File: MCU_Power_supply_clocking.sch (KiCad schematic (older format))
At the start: 60 parts, among them J2 OSTTC020162, J3 OSTTC020162, U10 TLV75529PDBV, U11 STM32H743ZIT6, U12 LD1117S33CTR, U13 LD1117S33CTR, U9 ST1L05APU33R, Y1 NX5032GA-8MHz, Y2 NX3215SA-32.768K-STD-MUA-14

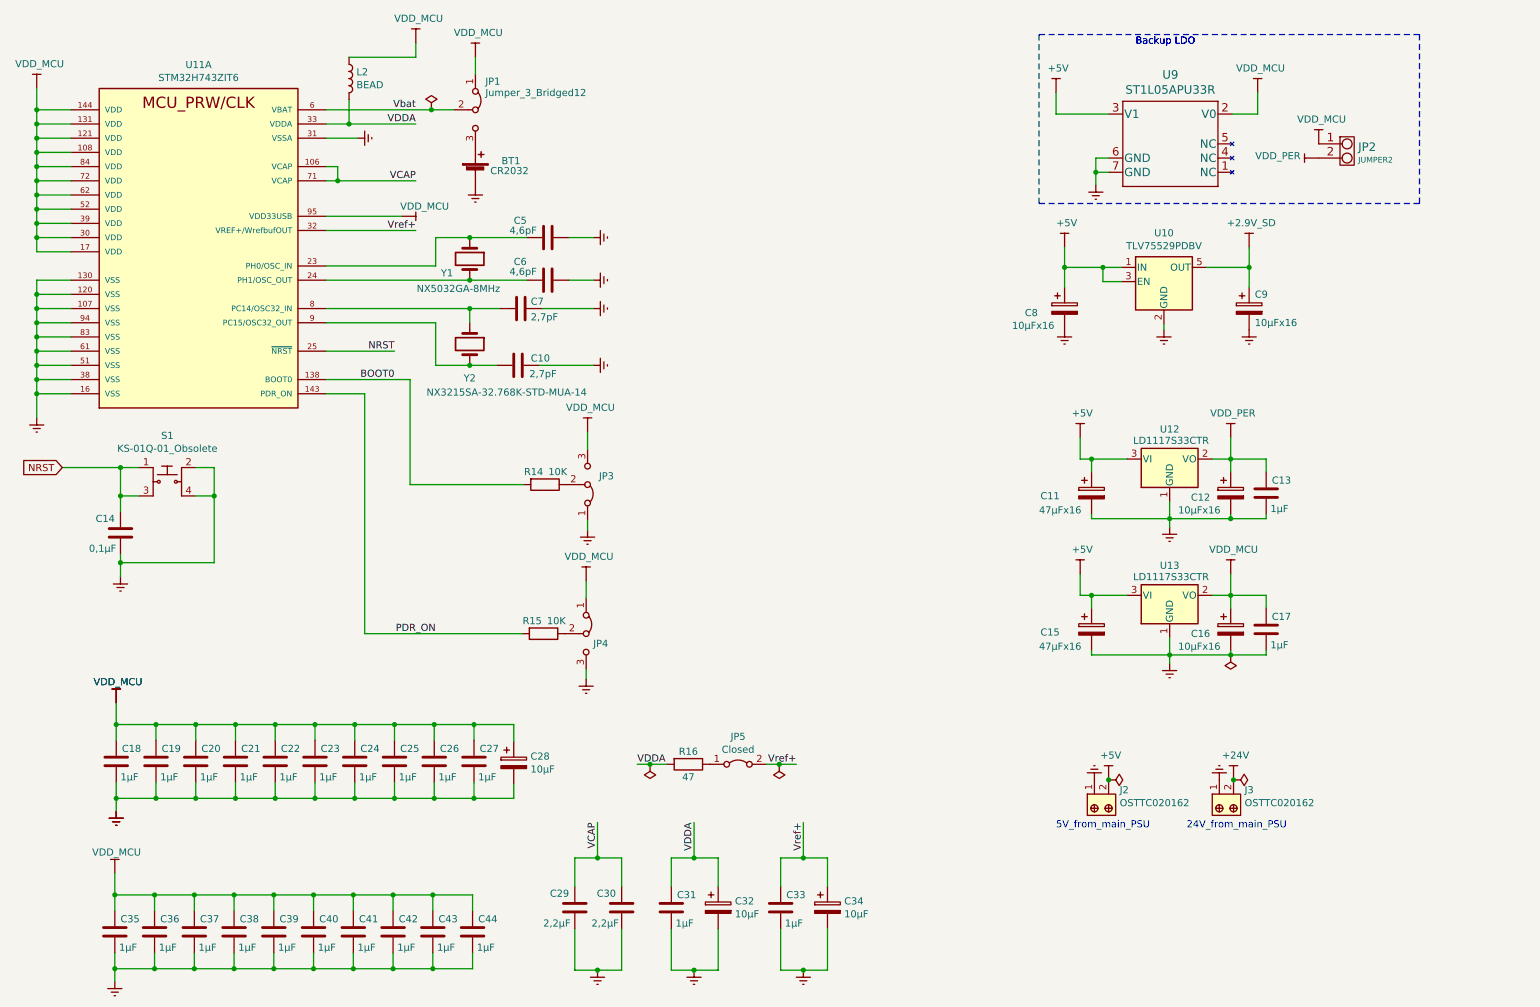
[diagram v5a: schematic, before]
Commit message: footprints associations is done
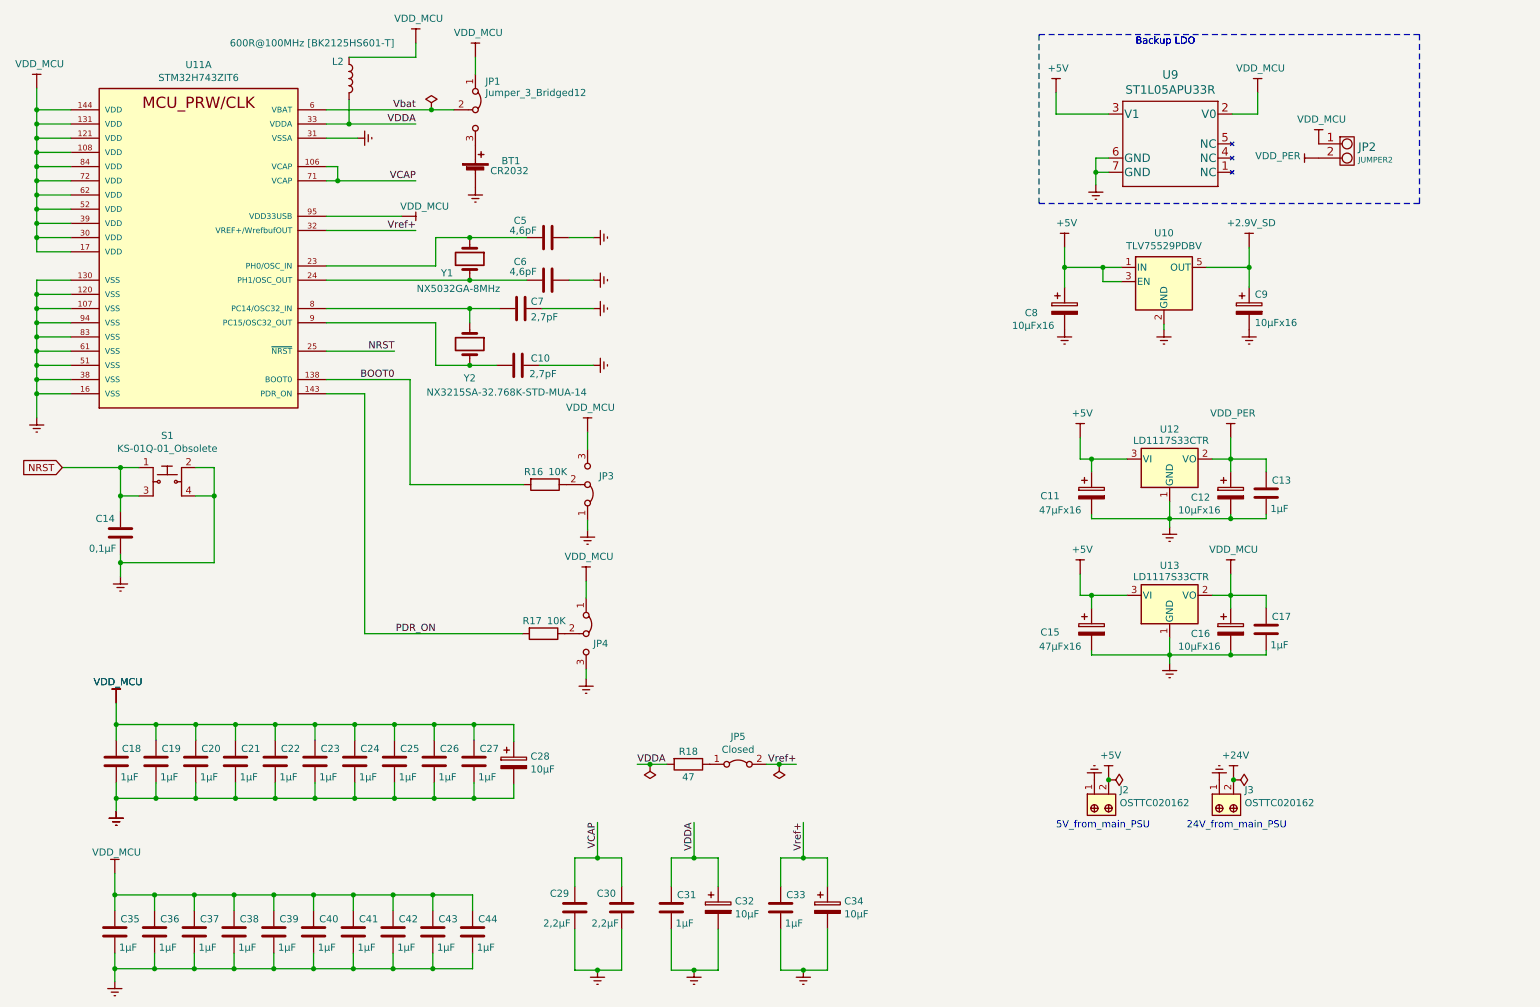
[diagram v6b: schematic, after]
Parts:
- C29, C30: footprint Capacitor_SMD:C_0805_2012Metric_Pad1.18x1.45mm_HandSolder -> Capacitor_SMD:C_0603_1608Metric_Pad1.08x0.95mm_HandSolder; Type C2012X7R1H225KT000E -> GRM188Z71E225KE43D
- JP1, JP4: footprint (none) -> Jumper:SolderJumper-3_P1.3mm_Open_RoundedPad1.0x1.5mm_NumberLabels
- JP2: footprint (none) -> Jumper:SolderJumper-2_P1.3mm_Open_TrianglePad1.0x1.5mm
- JP3: footprint (none) -> Connector_PinHeader_2.54mm:PinHeader_1x03_P2.54mm_Horizontal
- JP5: footprint (none) -> Jumper:SolderJumper-2_P1.3mm_Open_RoundedPad1.0x1.5mm
- L2: value BEAD -> 600R@100MHz [BK2125HS601-T]; footprint (none) -> Inductor_SMD:L_0805_2012Metric_Pad1.15x1.40mm_HandSolder
- U11: footprint QFP50P2200X2200X160-144N -> SVIELCOM:QFP50P2200X2200X160-144N
- U9: footprint DFN_5APU33R_STM -> SVIELCOM:ST1L05APU33R
- renumbered R14 to R16, R15 to R17, R16 to R18
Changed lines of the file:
@@
 Title "ШВУ"
 Date "2021-03-25"
-Rev "V0.1"
+Rev "V0.3"
 Comp "ЦВЕТМЕТНАЛАДКА"
 Comment1 "Шустов В.И."
@@
 F 0 "C29" H 4540 6770 50  0000 L CNN
 F 1 "2,2µF" H 4530 6980 50  0000 L CNN
-F 2 "Capacitor_SMD:C_0805_2012Metric_Pad1.18x1.45mm_HandSolder" H 4538 6720 50  0001 C CNN
+F 2 "Capacitor_SMD:C_0603_1608Metric_Pad1.08x0.95mm_HandSolder" H 4538 6720 50  0001 C CNN
 F 3 "" H 4500 6870 50  0001 C CNN
-F 4 "C2012X7R1H225KT000E" H 4500 6870 50  0001 C CNN "Type"
+F 4 "GRM188Z71E225KE43D" H 4500 6870 50  0001 C CNN "Type"
 	1    4500 6870
 	-1   0    0    1
@@
 F 0 "U11" H 1850 4267 50  0000 C CNN
 F 1 "STM32H743ZIT6" H 1850 4176 50  0000 C CNN
-F 2 "QFP50P2200X2200X160-144N" H 1900 4200 50  0001 L BNN
+F 2 "SVIELCOM:QFP50P2200X2200X160-144N" H 1900 4200 50  0001 L BNN
 F 3 "" H 1900 4600 50  0001 L BNN
 F 4 "STMicroelectronics" H 1900 4300 50  0001 L BNN "MANUFACTURER"
@@
 P 4290 3890
 AR Path="/60A0FE86" Ref="R?"  Part="1"
-AR Path="/60A03F8A/60A0FE86" Ref="R14"  Part="1"
-F 0 "R14" V 4200 3810 50  0000 C CNN
+AR Path="/60A03F8A/60A0FE86" Ref="R16"  Part="1"
+F 0 "R16" V 4200 3810 50  0000 C CNN
 F 1 "10K" V 4200 3980 50  0000 C CNN
 F 2 "Resistor_SMD:R_0805_2012Metric_Pad1.20x1.40mm_HandSolder" V 4220 3890 50  0001 C CNN
@@
 F 0 "C30" H 4870 6770 50  0000 L CNN
 F 1 "2,2µF" H 4850 6980 50  0000 L CNN
-F 2 "Capacitor_SMD:C_0805_2012Metric_Pad1.18x1.45mm_HandSolder" H 4868 6720 50  0001 C CNN
+F 2 "Capacitor_SMD:C_0603_1608Metric_Pad1.08x0.95mm_HandSolder" H 4868 6720 50  0001 C CNN
 F 3 "" H 4830 6870 50  0001 C CNN
-F 4 "C2012X7R1H225KT000E" H 4830 6870 50  0001 C CNN "Type"
+F 4 "GRM188Z71E225KE43D" H 4830 6870 50  0001 C CNN "Type"
 	1    4830 6870
 	-1   0    0    1
@@
 F 0 "JP1" V 3600 1320 50  0000 L CNN
 F 1 "Jumper_3_Bridged12" V 3680 1320 50  0000 L CNN
-F 2 "" H 3800 1250 50  0001 C CNN
+F 2 "Jumper:SolderJumper-3_P1.3mm_Open_RoundedPad1.0x1.5mm_NumberLabels" H 3800 1250 50  0001 C CNN
 F 3 "~" H 3800 1250 50  0001 C CNN
 	1    3800 1250
@@
 F 0 "JP3" V 4650 3970 50  0000 L CNN
 F 1 "Jumper_3_Bridged12" V 4580 3990 50  0001 L CNN
-F 2 "" H 4590 3890 50  0001 C CNN
+F 2 "Connector_PinHeader_2.54mm:PinHeader_1x03_P2.54mm_Horizontal" H 4590 3890 50  0001 C CNN
 F 3 "~" H 4590 3890 50  0001 C CNN
 	1    4590 3890
@@
 F 0 "JP5" H 5650 6055 50  0000 C CNN
 F 1 "Closed" H 5650 5964 50  0000 C CNN
-F 2 "" H 5650 5860 50  0001 C CNN
+F 2 "Jumper:SolderJumper-2_P1.3mm_Open_RoundedPad1.0x1.5mm" H 5650 5860 50  0001 C CNN
 F 3 "~" H 5650 5860 50  0001 C CNN
 	1    5650 5860
@@
 P 4280 4940
 AR Path="/60A0FEB9" Ref="R?"  Part="1"
-AR Path="/60A03F8A/60A0FEB9" Ref="R15"  Part="1"
-F 0 "R15" V 4190 4860 50  0000 C CNN
+AR Path="/60A03F8A/60A0FEB9" Ref="R17"  Part="1"
+F 0 "R17" V 4190 4860 50  0000 C CNN
 F 1 "10K" V 4190 5030 50  0000 C CNN
 F 2 "Resistor_SMD:R_0805_2012Metric_Pad1.20x1.40mm_HandSolder" V 4210 4940 50  0001 C CNN
@@
 F 0 "JP4" V 4650 4990 50  0000 L CNN
 F 1 "Jumper_3_Bridged12" V 4570 5040 50  0001 L CNN
-F 2 "" H 4580 4940 50  0001 C CNN
+F 2 "Jumper:SolderJumper-3_P1.3mm_Open_RoundedPad1.0x1.5mm_NumberLabels" H 4580 4940 50  0001 C CNN
 F 3 "~" H 4580 4940 50  0001 C CNN
 	1    4580 4940
@@
 F 0 "U9" H 8695 2177 60  0000 C CNN
 F 1 "ST1L05APU33R" H 8695 2071 60  0000 C CNN
-F 2 "DFN_5APU33R_STM" H 8860 2030 60  0001 C CNN
+F 2 "SVIELCOM:ST1L05APU33R" H 8860 2030 60  0001 C CNN
 F 3 "https://my.st.com/resource/en/datasheet/st1l05.pdf" H 8695 2071 60  0001 C CNN
 	1    8060 1590
@@
 F 0 "JP2" H 10018 1468 60  0000 L CNN
 F 1 "JUMPER2" H 10018 1377 40  0000 L CNN
-F 2 "" H 10040 1490 60  0001 C CNN
+F 2 "Jumper:SolderJumper-2_P1.3mm_Open_TrianglePad1.0x1.5mm" H 10040 1490 60  0001 C CNN
 F 3 "" H 10040 1490 60  0000 C CNN
 	1    10040 1490
@@
 P 5300 5860
 AR Path="/60D1EBF4" Ref="R?"  Part="1"
-AR Path="/60A03F8A/60D1EBF4" Ref="R16"  Part="1"
-F 0 "R16" V 5210 5860 50  0000 C CNN
+AR Path="/60A03F8A/60D1EBF4" Ref="R18"  Part="1"
+F 0 "R18" V 5210 5860 50  0000 C CNN
 F 1 "47" V 5390 5860 50  0000 C CNN
 F 2 "Resistor_SMD:R_0805_2012Metric_Pad1.20x1.40mm_HandSolder" V 5230 5860 50  0001 C CNN
@@
 AR Path="/60A0FE91" Ref="L?"  Part="1"
 AR Path="/60A03F8A/60A0FE91" Ref="L2"  Part="1"
-F 0 "L2" H 2962 1076 50  0000 L CNN
-F 1 "BEAD" H 2962 985 50  0000 L CNN
-F 2 "" H 2910 1030 50  0001 C CNN
+F 0 "L2" H 2790 1150 50  0000 L CNN
+F 1 "600R@100MHz [BK2125HS601-T]" H 2070 1280 50  0000 L CNN
+F 2 "Inductor_SMD:L_0805_2012Metric_Pad1.15x1.40mm_HandSolder" H 2910 1030 50  0001 C CNN
 F 3 "~" H 2910 1030 50  0001 C CNN
 	1    2910 1030
@@
 	3020 4940 4130 4940
 $Comp
-L power:PWR_FLAG #FLG08
+L power:PWR_FLAG #FLG07
 U 1 1 610DFDF1
 P 8260 5970
-F 0 "#FLG08" H 8260 6045 50  0001 C CNN
+F 0 "#FLG07" H 8260 6045 50  0001 C CNN
 F 1 "PWR_FLAG" V 8260 6098 50  0001 L CNN
 F 2 "" H 8260 5970 50  0001 C CNN
@@
 Connection ~ 8260 5970
 $Comp
-L power:PWR_FLAG #FLG09
+L power:PWR_FLAG #FLG08
 U 1 1 610E04FC
 P 9140 5970
-F 0 "#FLG09" H 9140 6045 50  0001 C CNN
+F 0 "#FLG08" H 9140 6045 50  0001 C CNN
 F 1 "PWR_FLAG" V 9140 6098 50  0001 L CNN
 F 2 "" H 9140 5970 50  0001 C CNN
@@
 $EndComp
 Connection ~ 9140 5970
-$Comp
-L power:PWR_FLAG #FLG05
-U 1 1 6111D84B
-P 9120 5090
-F 0 "#FLG05" H 9120 5165 50  0001 C CNN
-F 1 "PWR_FLAG" H 9100 5270 50  0001 C CNN
-F 2 "" H 9120 5090 50  0001 C CNN
-F 3 "~" H 9120 5090 50  0001 C CNN
-	1    9120 5090
-	-1   0    0    1
-$EndComp
 $Comp
 L power:PWR_FLAG #FLG04
@@
 	3490 1250 3650 1250
 $Comp
-L power:PWR_FLAG #FLG07
+L power:PWR_FLAG #FLG06
 U 1 1 61150D1F
 P 5940 5860
-F 0 "#FLG07" H 5940 5935 50  0001 C CNN
+F 0 "#FLG06" H 5940 5935 50  0001 C CNN
 F 1 "PWR_FLAG" V 5940 5988 50  0001 L CNN
 F 2 "" H 5940 5860 50  0001 C CNN
@@
 	5940 5860 5850 5860
 $Comp
-L power:PWR_FLAG #FLG06
+L power:PWR_FLAG #FLG05
 U 1 1 61180CD3
 P 5030 5860
-F 0 "#FLG06" H 5030 5935 50  0001 C CNN
+F 0 "#FLG05" H 5030 5935 50  0001 C CNN
 F 1 "PWR_FLAG" V 5030 5988 50  0001 L CNN
 F 2 "" H 5030 5860 50  0001 C CNN

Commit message: corrected few footprints, correct all resistors and capacitors type for ordering
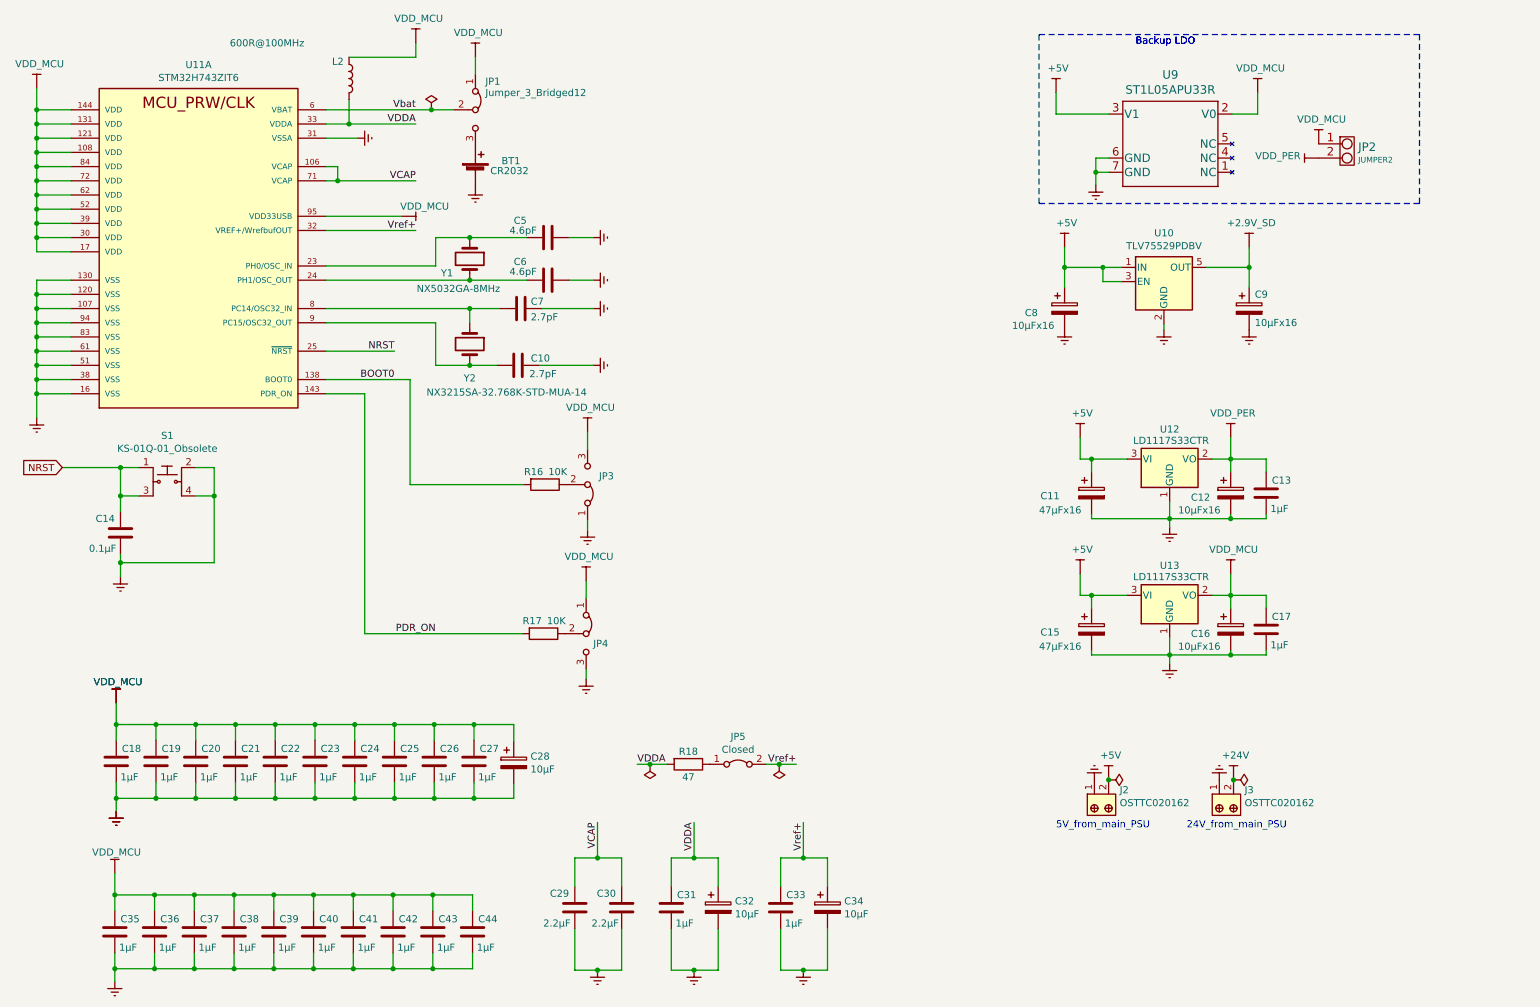
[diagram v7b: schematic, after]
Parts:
- C10, C7: value 2,7pF -> 2.7pF
- C14: value 0,1µF -> 0.1µF; Type (none) -> CL10B104KC8NNNC
- C29, C30: value 2,2µF -> 2.2µF
- C5, C6: value 4,6pF -> 4.6pF; Type (none) -> CC0603CRNPO9BN4R7
- L2: value 600R@100MHz [BK2125HS601-T] -> 600R@100MHz; Type (none) -> BK2125HS601-T
- R16, R17: Type (none) -> RC0805FR-0710KL
- R18: Type (none) -> RC0805FR-0747RL
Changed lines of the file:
@@
 AR Path="/60A03F8A/60A0FE7B" Ref="C5"  Part="1"
 F 0 "C5" V 4190 1910 50  0000 L CNN
-F 1 "4,6pF" V 4260 1880 50  0000 L CNN
+F 1 "4.6pF" V 4260 1880 50  0000 L CNN
 F 2 "Capacitor_SMD:C_0603_1608Metric_Pad1.08x0.95mm_HandSolder" H 4348 2000 50  0001 C CNN
 F 3 "" H 4310 2150 50  0001 C CNN
-F 4 "" H 4310 2150 50  0001 C CNN "Type"
+F 4 "CC0603CRNPO9BN4R7" H 4310 2150 50  0001 C CNN "Type"
 	1    4310 2150
 	0    1    1    0
@@
 AR Path="/60A03F8A/60A0FE7C" Ref="C29"  Part="1"
 F 0 "C29" H 4540 6770 50  0000 L CNN
-F 1 "2,2µF" H 4530 6980 50  0000 L CNN
+F 1 "2.2µF" H 4530 6980 50  0000 L CNN
 F 2 "Capacitor_SMD:C_0603_1608Metric_Pad1.08x0.95mm_HandSolder" H 4538 6720 50  0001 C CNN
 F 3 "" H 4500 6870 50  0001 C CNN
@@
 AR Path="/60A03F8A/60A2F6CF" Ref="C6"  Part="1"
 F 0 "C6" V 4180 2210 50  0000 L CNN
-F 1 "4,6pF" V 4250 2180 50  0000 L CNN
+F 1 "4.6pF" V 4250 2180 50  0000 L CNN
 F 2 "Capacitor_SMD:C_0603_1608Metric_Pad1.08x0.95mm_HandSolder" H 4348 2300 50  0001 C CNN
 F 3 "" H 4310 2450 50  0001 C CNN
-F 4 "" H 4310 2450 50  0001 C CNN "Type"
+F 4 "CC0603CRNPO9BN4R7" H 4310 2450 50  0001 C CNN "Type"
 	1    4310 2450
 	0    1    1    0
@@
 AR Path="/60A03F8A/60A2F6F0" Ref="C7"  Part="1"
 F 0 "C7" V 4070 2720 50  0000 L CNN
-F 1 "2,7pF" V 4180 2720 50  0000 L CNN
+F 1 "2.7pF" V 4180 2720 50  0000 L CNN
 F 2 "Capacitor_SMD:C_0603_1608Metric_Pad1.08x0.95mm_HandSolder" H 4158 2500 50  0001 C CNN
 F 3 "https://www.mouser.com/ds/2/447/Yageo_UPY-GP_NP0_16V-to-50V_9-1211922.pdf" H 4120 2650 50  0001 C CNN
@@
 AR Path="/60A03F8A/60A2F6F7" Ref="C10"  Part="1"
 F 0 "C10" V 4050 3140 50  0000 L CNN
-F 1 "2,7pF" V 4160 3130 50  0000 L CNN
+F 1 "2.7pF" V 4160 3130 50  0000 L CNN
 F 2 "Capacitor_SMD:C_0603_1608Metric_Pad1.08x0.95mm_HandSolder" H 4138 2900 50  0001 C CNN
 F 3 "https://www.mouser.com/ds/2/447/Yageo_UPY-GP_NP0_16V-to-50V_9-1211922.pdf" H 4100 3050 50  0001 C CNN
@@
 F 2 "Resistor_SMD:R_0805_2012Metric_Pad1.20x1.40mm_HandSolder" V 4220 3890 50  0001 C CNN
 F 3 "~" H 4290 3890 50  0001 C CNN
+F 4 "RC0805FR-0710KL" V 4290 3890 50  0001 C CNN "Type"
 	1    4290 3890
 	0    1    1    0
@@
 AR Path="/60A03F8A/60A2F795" Ref="C30"  Part="1"
 F 0 "C30" H 4870 6770 50  0000 L CNN
-F 1 "2,2µF" H 4850 6980 50  0000 L CNN
+F 1 "2.2µF" H 4850 6980 50  0000 L CNN
 F 2 "Capacitor_SMD:C_0603_1608Metric_Pad1.08x0.95mm_HandSolder" H 4868 6720 50  0001 C CNN
 F 3 "" H 4830 6870 50  0001 C CNN
@@
 AR Path="/60A03F8A/60A0FE99" Ref="C14"  Part="1"
 F 0 "C14" H 1340 4130 50  0000 L CNN
-F 1 "0,1µF" H 1330 4340 50  0000 L CNN
+F 1 "0.1µF" H 1330 4340 50  0000 L CNN
 F 2 "Capacitor_SMD:C_0603_1608Metric_Pad1.08x0.95mm_HandSolder" H 1338 4080 50  0001 C CNN
 F 3 "" H 1300 4230 50  0001 C CNN
-F 4 "" H 1300 4230 50  0001 C CNN "Type"
+F 4 "CL10B104KC8NNNC" H 1300 4230 50  0001 C CNN "Type"
 	1    1300 4230
 	-1   0    0    1
@@
 F 2 "Resistor_SMD:R_0805_2012Metric_Pad1.20x1.40mm_HandSolder" V 4210 4940 50  0001 C CNN
 F 3 "~" H 4280 4940 50  0001 C CNN
+F 4 "RC0805FR-0710KL" V 4280 4940 50  0001 C CNN "Type"
 	1    4280 4940
 	0    1    1    0
@@
 F 2 "Resistor_SMD:R_0805_2012Metric_Pad1.20x1.40mm_HandSolder" V 5230 5860 50  0001 C CNN
 F 3 "~" H 5300 5860 50  0001 C CNN
+F 4 "RC0805FR-0747RL" V 5300 5860 50  0001 C CNN "Type"
 	1    5300 5860
 	0    1    1    0
@@
 AR Path="/60A03F8A/60A0FE91" Ref="L2"  Part="1"
 F 0 "L2" H 2790 1150 50  0000 L CNN
-F 1 "600R@100MHz [BK2125HS601-T]" H 2070 1280 50  0000 L CNN
+F 1 "600R@100MHz" H 2070 1280 50  0000 L CNN
 F 2 "Inductor_SMD:L_0805_2012Metric_Pad1.15x1.40mm_HandSolder" H 2910 1030 50  0001 C CNN
 F 3 "~" H 2910 1030 50  0001 C CNN
+F 4 "BK2125HS601-T" H 2910 1030 50  0001 C CNN "Type"
 	1    2910 1030
 	1    0    0    -1
